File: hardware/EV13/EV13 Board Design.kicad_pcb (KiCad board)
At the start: 4 copper layers, 66 x 99.3 mm, 149 parts, among them CN2 Conn_05x02_Female, CN3 Conn_01x06_Female, CN4 Conn_01x06_Female, CN5 Conn_02x05_Male, CN6 Conn_02x05_Male, CN7 Conn_02x05_Male, J1 Conn_01x02_Socket, J10 Conn_01x08_Socket, J2 AudioJack1, J3 Conn_01x06_Socket, J9 USB_C_Receptacle, SW1 SW_Push, SW3 SW_Push, SW4 SW_Push, SW5 SW_Push, SW6 SW_SPDT, U1 STM32F405RGTx, U11 ESP32-S3-WROOM-1, U13 BM14B(0.8)-24DS-0.4V(53), U2 BQ21040DBV, U3 CH340C, U4 USBLC6-2P6, U5 M24C02-RMN6TP, U6 WM8960CGEFL/RV, U7 TPS63060, U8 STM32F072CBTx, Y1 Crystal_GND24

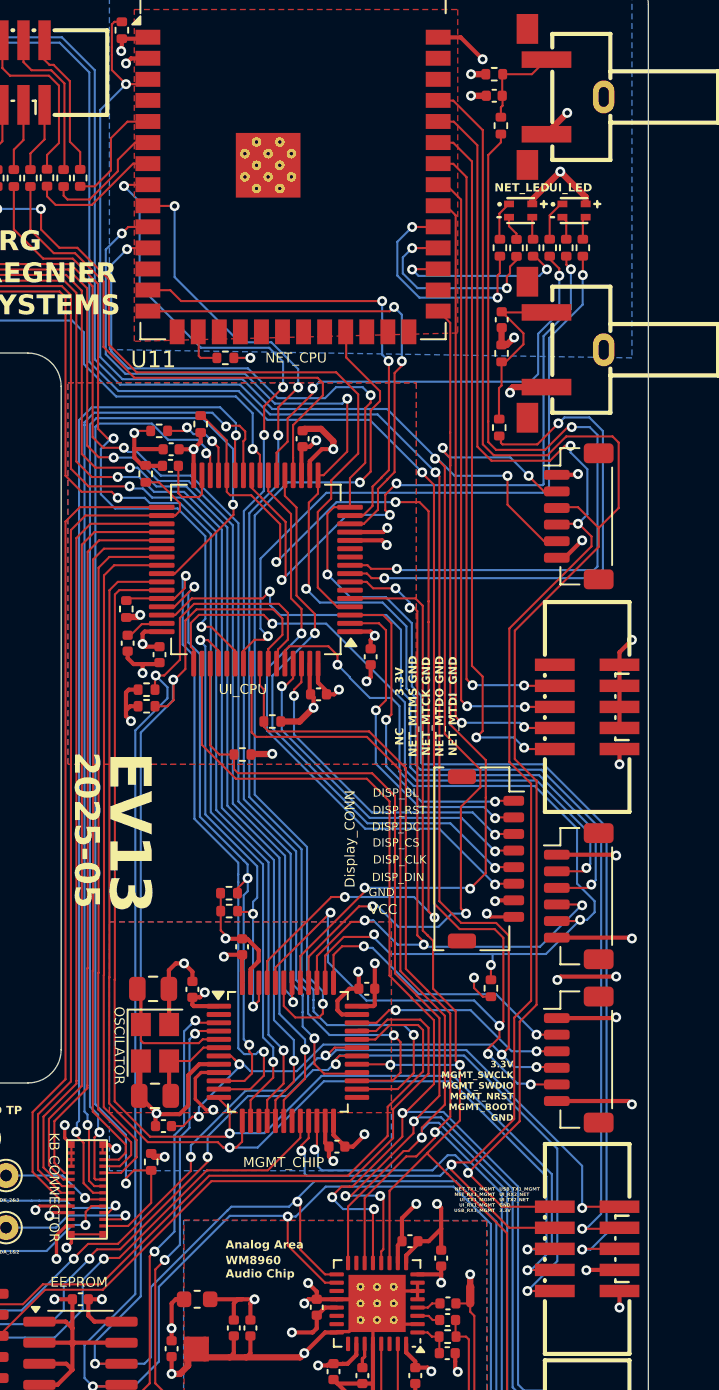
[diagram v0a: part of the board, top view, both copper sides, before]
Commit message: Added pull down resistors to unused MGMT pins
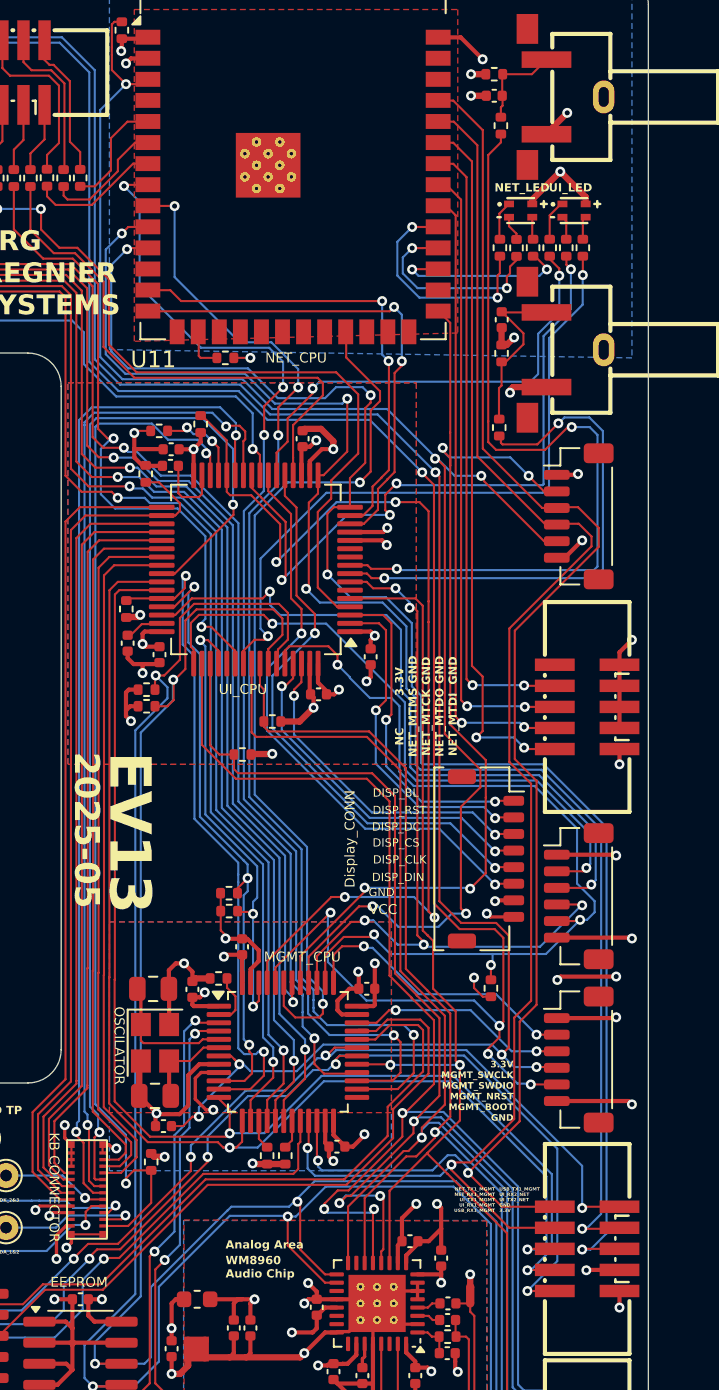
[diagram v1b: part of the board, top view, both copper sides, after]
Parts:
- added R57: 4k7, Resistor_SMD:R_0402_1005Metric, F.Cu at (158.1, 117.4)
- added R58: 4k7, Resistor_SMD:R_0402_1005Metric, F.Cu at (154.1, 106.7)
- added R59: 4k7, Resistor_SMD:R_0402_1005Metric, F.Cu at (157.0, 117.4)
- L2: value 120R1 -> 120Ω
- R11, R12, R15, R17, R18, R24, R25: value 150R -> 150
- R16, R23: value 180R -> 180
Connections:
- U8 pad 15: unconnected-(U8-PA5-Pad15) -> Net-(U8-PA5)
- U8 pad 19: unconnected-(U8-PB1-Pad19) -> Net-(U8-PB1)
- U8 pad 2: unconnected-(U8-PC13-Pad2) -> Net-(U8-PC13)
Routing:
- net /NET_TX1_MGMT: track 102.4 -> 93.8 mm
- net GND: track 663.4 -> 671.9 mm, vias 83 -> 84
- net /NET_RX1_MGMT: track 99.2 -> 94.0 mm, vias 4 -> 2
- net Net-(U8-PC13): track 0.00 -> 3.23 mm
- net Net-(U8-PA5): track 0.00 -> 1.79 mm
- net Net-(U8-PB1): track 0.00 -> 1.75 mm
- net /I2S_DACLRC: track 79.6 -> 80.9 mm
- net /I2S_BCLK: track 79.6 -> 80.7 mm
- net /USB_DTR_MGMT: track 29.5 -> 30.6 mm
- net /NET_NRST: track 98.8 -> 97.8 mm
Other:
- board text added: "MGMT_CPU"
- board text removed: "MGMT_CHIP"

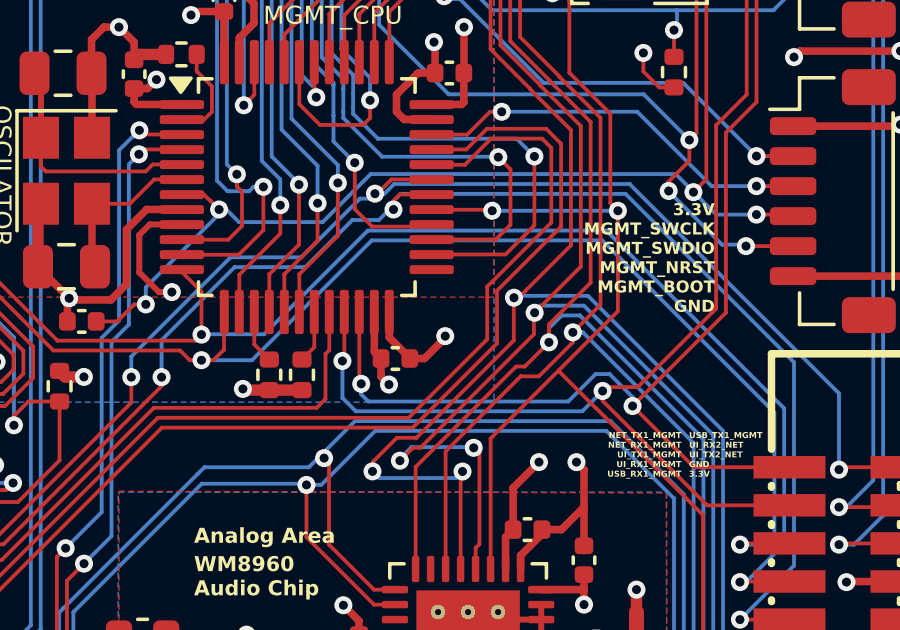
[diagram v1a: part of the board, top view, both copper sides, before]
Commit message: Added pull down resistors to unused MGMT pins
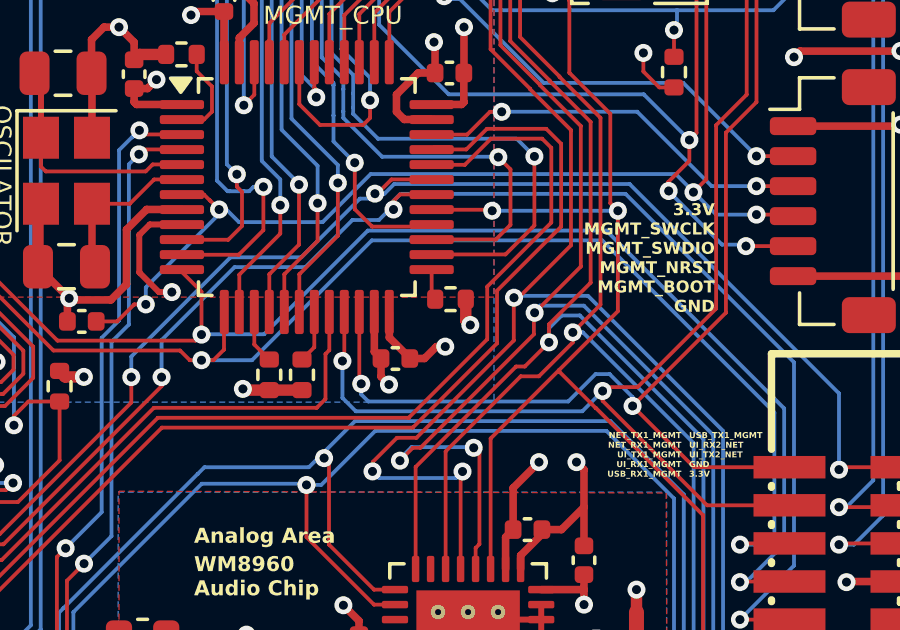
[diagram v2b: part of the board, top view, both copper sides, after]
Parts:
- added R60: 4k7, Resistor_SMD:R_0402_1005Metric, F.Cu at (163.1, 114.9)
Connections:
- U8 pad 25: unconnected-(U8-PB12-Pad25) -> Net-(U8-PB12)
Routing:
- net Net-(U8-PB12): track 0.00 -> 1.04 mm
- net GND: track 671.9 -> 672.8 mm, vias 84 -> 85

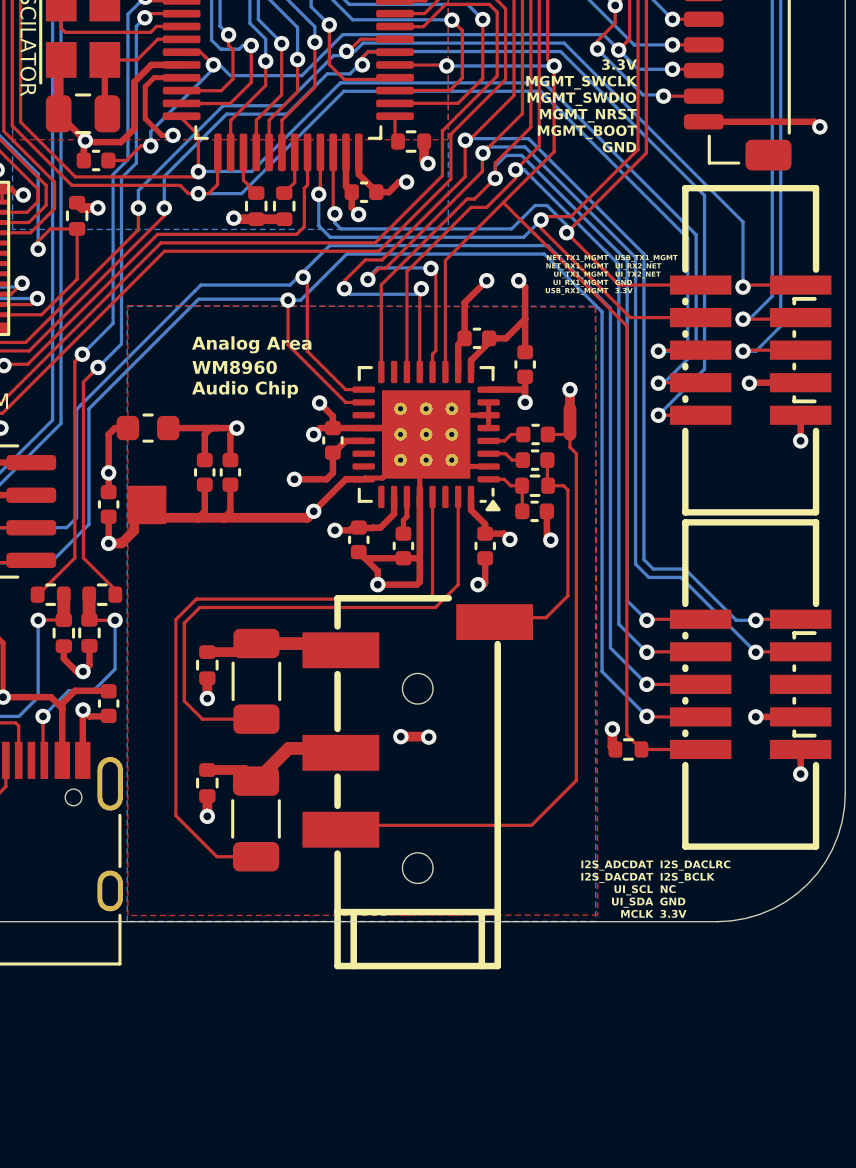
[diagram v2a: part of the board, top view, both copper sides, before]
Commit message: Added dual HP jack setup
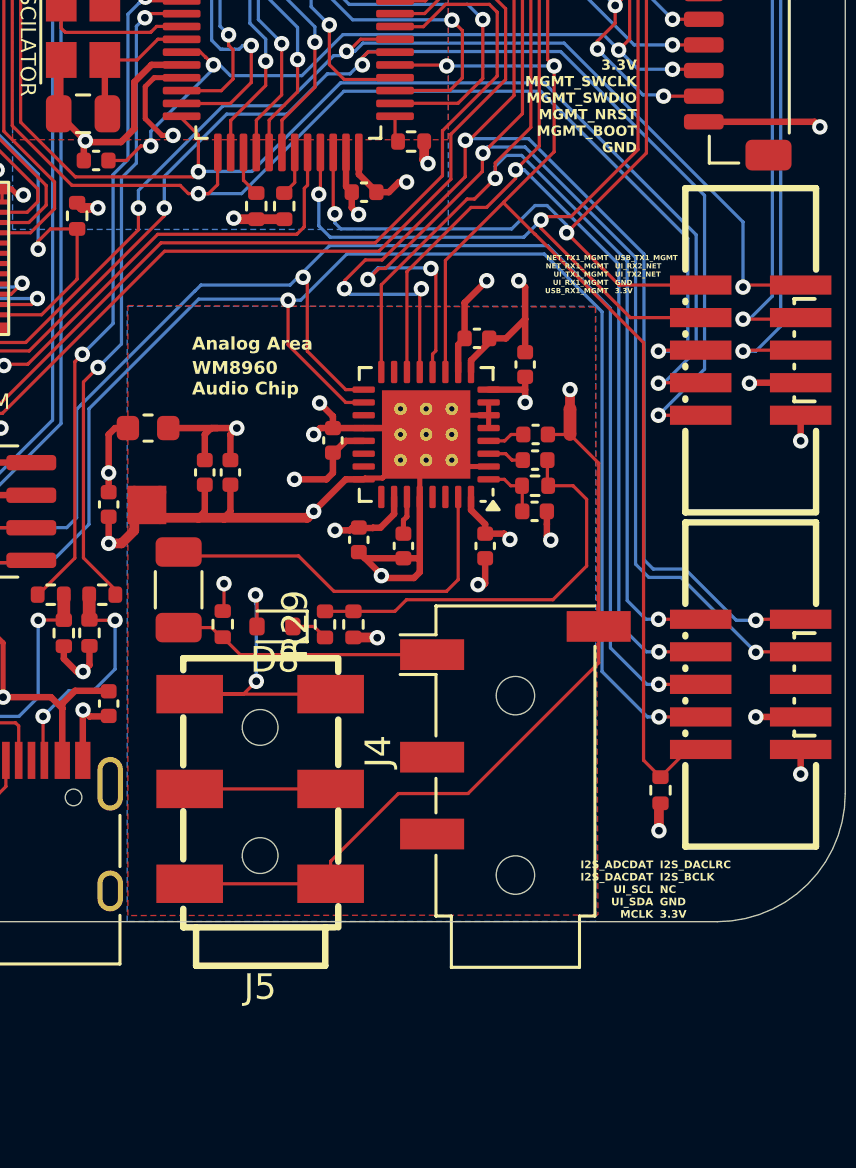
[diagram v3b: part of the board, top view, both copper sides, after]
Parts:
- removed C29: 100u, Capacitor_SMD:C_1206_3216Metric
- removed J2: AudioJack1, Hactar_Footprints:AUDIO-SMD_PJ-320D
- added D8: 1N4148WT, Diode_SMD:D_SOD-523, F.Cu at (157.7, 133.8)
- added J4: AudioJack2, Connector_Audio:Jack_3.5mm_PJ320D_Horizontal, F.Cu at (167.1, 138.7)
- added J5: AudioJack3, Hactar_Footprints:AUDIO-SMD_PJ-242, F.Cu at (157.2, 140.1)
- added R29: 51k, Resistor_SMD:R_0402_1005Metric, F.Cu at (159.7, 133.7)
- R56: value 4k7 -> 110k
- moved R56 8.41 mm to (160.8, 133.7), turned to -90 degrees
- moved C30 4.69 mm to (154.0, 132.3), turned to -90 degrees
- moved R50 2.02 mm to (172.8, 140.2), turned to 90 degrees
- moved R55 1.71 mm to (155.7, 133.7), turned to -90 degrees
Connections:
- R56 pad 1: GNDA -> /MIC_P
- R56 pad 2: /HP_R -> GNDA
- U6 pad 29: Net-(U6-HP_R) -> unconnected-(U6-HP_R-Pad29)
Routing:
- net Net-(U6-HP_R): track 25.7 -> 0.00 mm
- net GNDA: track 107.1 -> 93.2 mm, vias 12 -> 10
- net Net-(D8-A): track 0.00 -> 12.9 mm, vias 0 -> 2
- net /MIC_P: track 9.34 -> 16.3 mm
- net /HP_R: track 5.99 -> 0.00 mm
- net Net-(U6-HP_L): track 20.9 -> 15.0 mm
- net /MIC_N: track 24.5 -> 30.3 mm
- net unconnected-(J5-PadR)_1: track 0.00 -> 5.50 mm
- net /HP_L: track 4.89 -> 10.3 mm
- net Net-(D8-K): track 0.00 -> 1.43 mm
- net /MCLK: track 79.0 -> 80.1 mm

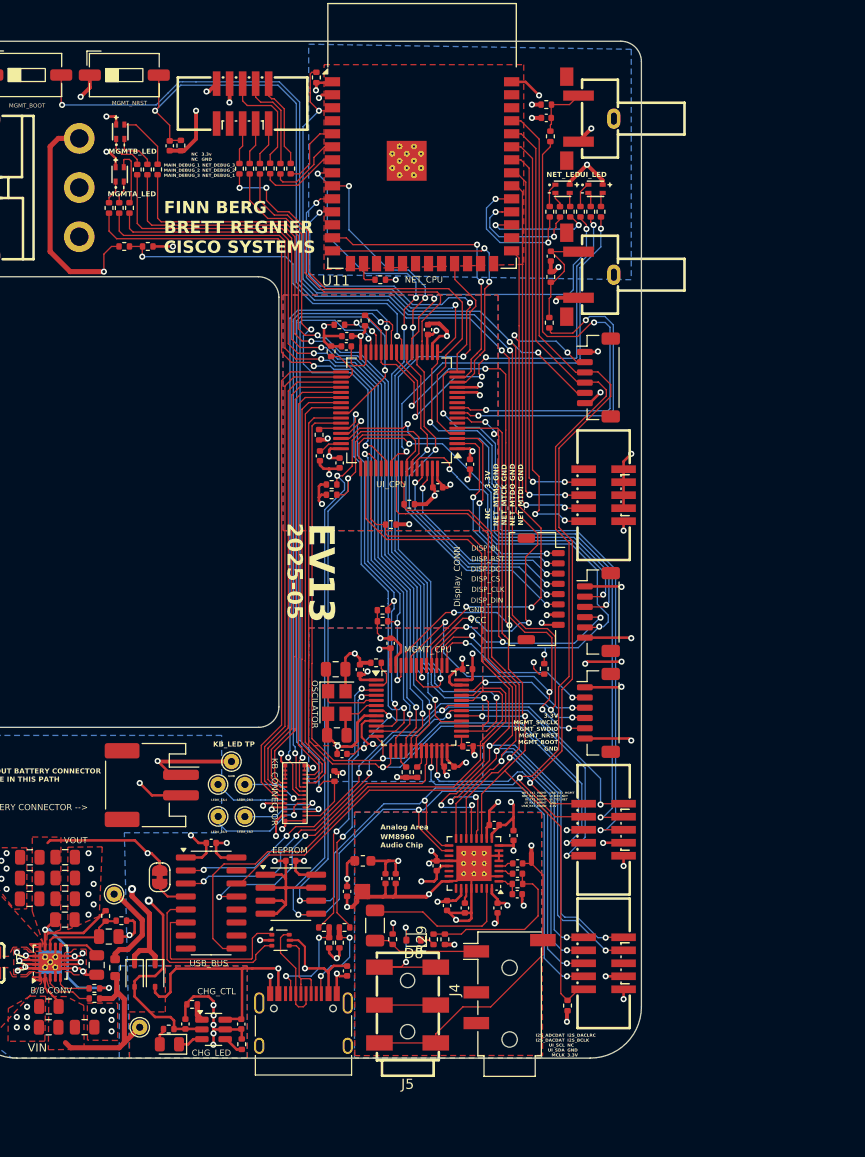
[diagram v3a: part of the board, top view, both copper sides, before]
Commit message: Dev board with dual headset and 2mm display connector
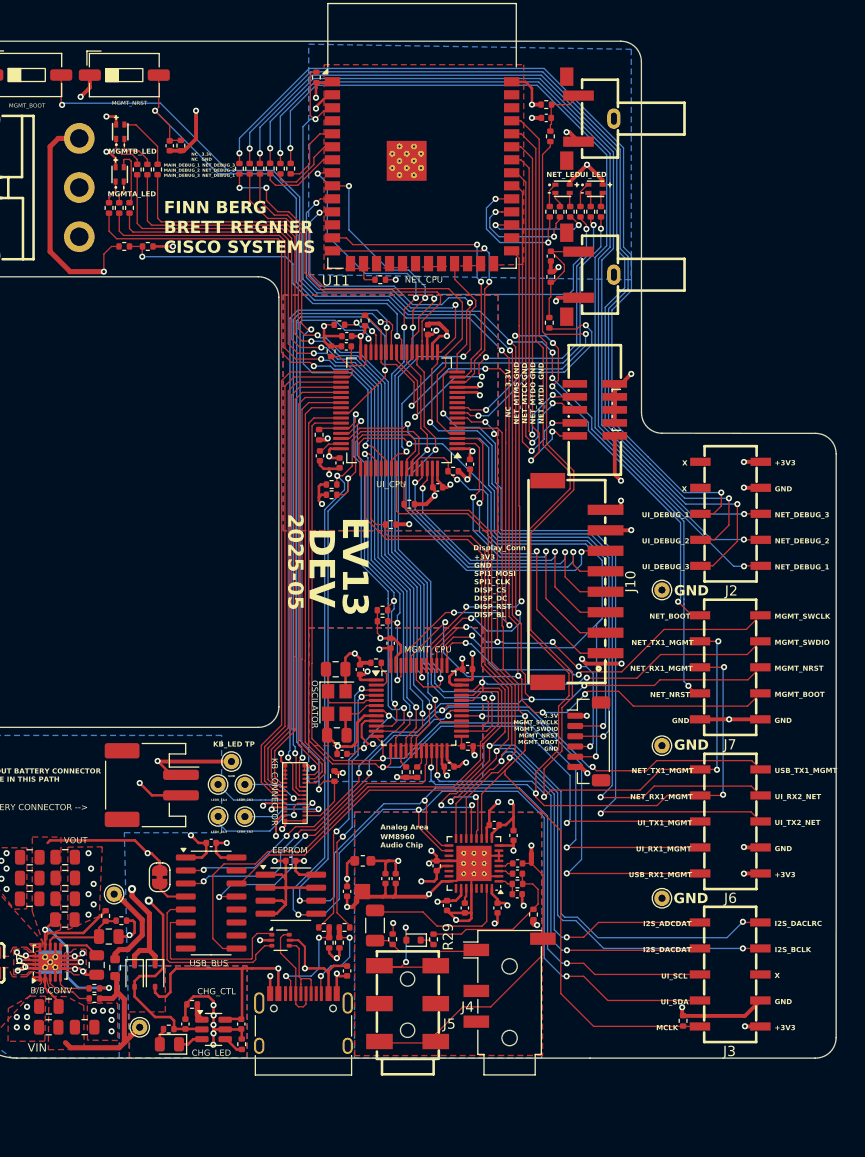
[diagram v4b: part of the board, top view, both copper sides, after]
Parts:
- removed CN3: Conn_01x06_Female, Connector_JST:JST_SH_BM06B-SRSS-TB_1x06-1MP_P1.00mm_Vertical
- removed CN5, CN6, CN7: Conn_02x05_Male, Hactar_Footprints:IDC-SMD_10P-P1.27_X1270WVS-2X05B-6TV01
- added J2: Conn_02x05_Counter_Clockwise, Hactar_Footprints:HDR-SMD_10P-P2.54, F.Cu at (188.7, 92.2)
- added J6: Conn_02x05_Counter_Clockwise, Hactar_Footprints:HDR-SMD_10P-P2.54, F.Cu at (188.7, 122.2)
- added J7: Conn_02x05_Counter_Clockwise, Hactar_Footprints:HDR-SMD_10P-P2.54, F.Cu at (188.7, 107.1)
- added TP10: TestPoint, TestPoint:TestPoint_THTPad_D1.5mm_Drill0.7mm, F.Cu at (182.0, 99.6)
- added TP11: TestPoint, TestPoint:TestPoint_THTPad_D1.5mm_Drill0.7mm, F.Cu at (182.0, 129.7)
- added TP9: TestPoint, TestPoint:TestPoint_THTPad_D1.5mm_Drill0.7mm, F.Cu at (182.0, 114.8)
- J10: footprint Connector_JST:JST_SHL_SM08B-SHLS-TF_1x08-1MP_P1.00mm_Horizontal -> Hactar_Footprints:CONN-SMD_8P-P2.00_S8B-PH-SM4-TB-LF-SN
- J3: value Conn_01x06_Socket -> Conn_02x05_Counter_Clockwise; footprint Connector_JST:JST_SH_BM06B-SRSS-TB_1x06-1MP_P1.00mm_Vertical -> Hactar_Footprints:HDR-SMD_10P-P2.54
- moved J3 59.7 mm to (188.7, 137.1), turned to 90 degrees
- moved R54 21.2 mm to (161.6, 88.0), turned to 0 degrees
- moved CN4 12.7 mm to (174.9, 114.4)
- moved R50 11.4 mm to (184.1, 141.7), turned to -90 degrees
- moved R56 8.98 mm to (169.5, 131.3)
- moved CN2 8.37 mm to (175.4, 82.0)
- moved J10 3.54 mm to (173.7, 98.8)
- moved J4 0.14 mm to (167.1, 138.6)
- moved J5 0.14 mm to (157.2, 140.0)
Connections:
- J3 pad 2: /NET_BOOT -> GND
- J3 pad 3: /NET_TX1_MGMT -> unconnected-(J3-Pin_3-Pad3)
- J3 pad 4: /NET_RX1_MGMT -> /I2S_BCLK
- J3 pad 5: /NET_NRST -> /I2S_DACLRC
- J3 pad 6: GND -> /I2S_ADCDAT
- R56 pad 2: GNDA -> GND
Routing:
- net Net-(J2-Pin_5): track 4.25 -> 95.7 mm, vias 0 -> 2
- net Net-(J2-Pin_4): track 4.14 -> 93.4 mm, vias 0 -> 2
- net Net-(J2-Pin_3): track 4.03 -> 91.0 mm, vias 0 -> 2
- net Net-(J2-Pin_6): track 8.83 -> 88.8 mm, vias 0 -> 2
- net Net-(J2-Pin_7): track 9.54 -> 88.7 mm, vias 0 -> 2
- net Net-(J2-Pin_8): track 10.9 -> 88.6 mm, vias 0 -> 2
- net /NET_NRST: track 97.8 -> 131.0 mm, vias 5 -> 7
- net +3.3V: track 498.0 -> 528.3 mm, vias 37 -> 35
- net /NET_TX1_MGMT: track 93.8 -> 120.0 mm, vias 2 -> 4
- net /NET_BOOT: track 59.4 -> 85.7 mm, vias 4 -> 6
- net /NET_RX1_MGMT: track 94.0 -> 119.9 mm, vias 2 -> 4
- net /MGMT_SWCLK: track 17.2 -> 36.2 mm
- net /MGMT_SWDIO: track 13.1 -> 31.4 mm
- net /UI_SWCLK: track 38.6 -> 53.2 mm
- net /UI_SWDIO: track 43.5 -> 57.6 mm
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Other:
- board size 66 x 99.3 mm -> 85 x 99.3 mm
- board text added: "+3V3"
- board text added: "+3V3 GND SPI1_MOSI SPI1_CLK DISP_CS DISP_DC DISP_RST DISP_BL"
- board text added: "DEV"
- board text added: "Display_Conn"
- board text added: "I2S_ADCDAT"
- board text added: "I2S_BCLK"
- board text added: "I2S_DACDAT"
- board text added: "I2S_DACLRC"
- board text added: "MCLK"
- board text added: "MGMT_SWCLK"
- board text added: "MGMT_SWDIO"
- board text added: "NET_BOOT"
- board text added: "NET_NRST"
- board text added: "NET_RX1_MGMT"
- board text added: "NET_TX1_MGMT"
- board text added: "UI_DEBUG_1"
- board text added: "UI_DEBUG_2"
- board text added: "UI_DEBUG_3"
- board text added: "UI_RX1_MGMT"
- board text added: "UI_RX2_NET"
- board text added: "UI_SCL"
- board text added: "UI_SDA"
- board text added: "UI_TX1_MGMT"
- board text added: "UI_TX2_NET"
- board text added: "USB_RX1_MGMT"
- board text added: "USB_TX1_MGMT"
- board text added: "X"
- board text removed: "DISP_BL"
- board text removed: "DISP_CLK"
- board text removed: "DISP_CS"
- board text removed: "DISP_DC"
- board text removed: "DISP_DIN"
- board text removed: "DISP_RST"
- board text removed: "Display_CONN"
- board text removed: "I2S_ADCDAT I2S_DACDAT UI_SCL UI_SDA MCLK"
- board text removed: "I2S_DACLRC I2S_BCLK NC GND 3.3V"
- board text removed: "NET_TX1_MGMT NET_RX1_MGMT UI_TX1_MGMT UI_RX1_MGMT USB_RX1_MGMT"
- board text removed: "USB_TX1_MGMT UI_RX2_NET UI_TX2_NET GND 3.3V"
- board text removed: "VCC"
